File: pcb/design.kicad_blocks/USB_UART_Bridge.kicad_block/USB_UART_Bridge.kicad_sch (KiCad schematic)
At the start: 17 parts, among them J1 614105150721, U2 MCP2221A-I/ST, U3 AP2112K-3.3

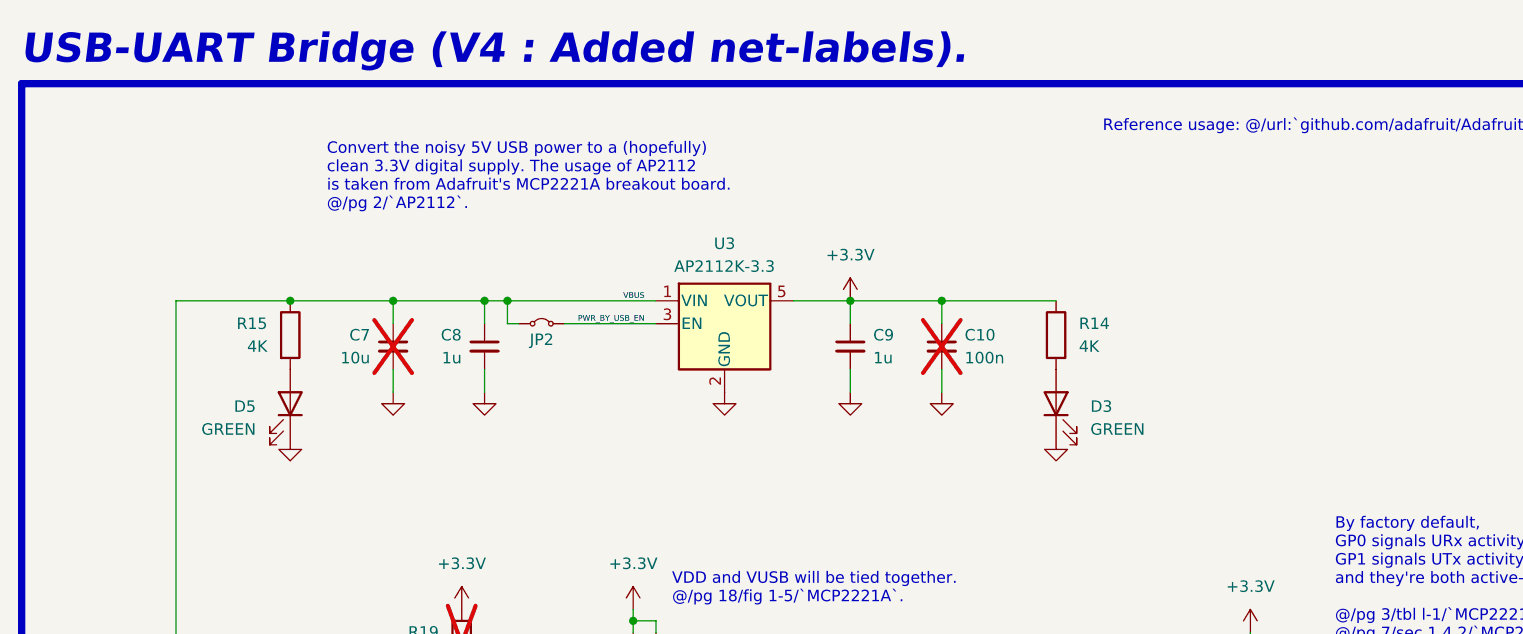
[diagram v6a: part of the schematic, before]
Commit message: Placed down most of the components.
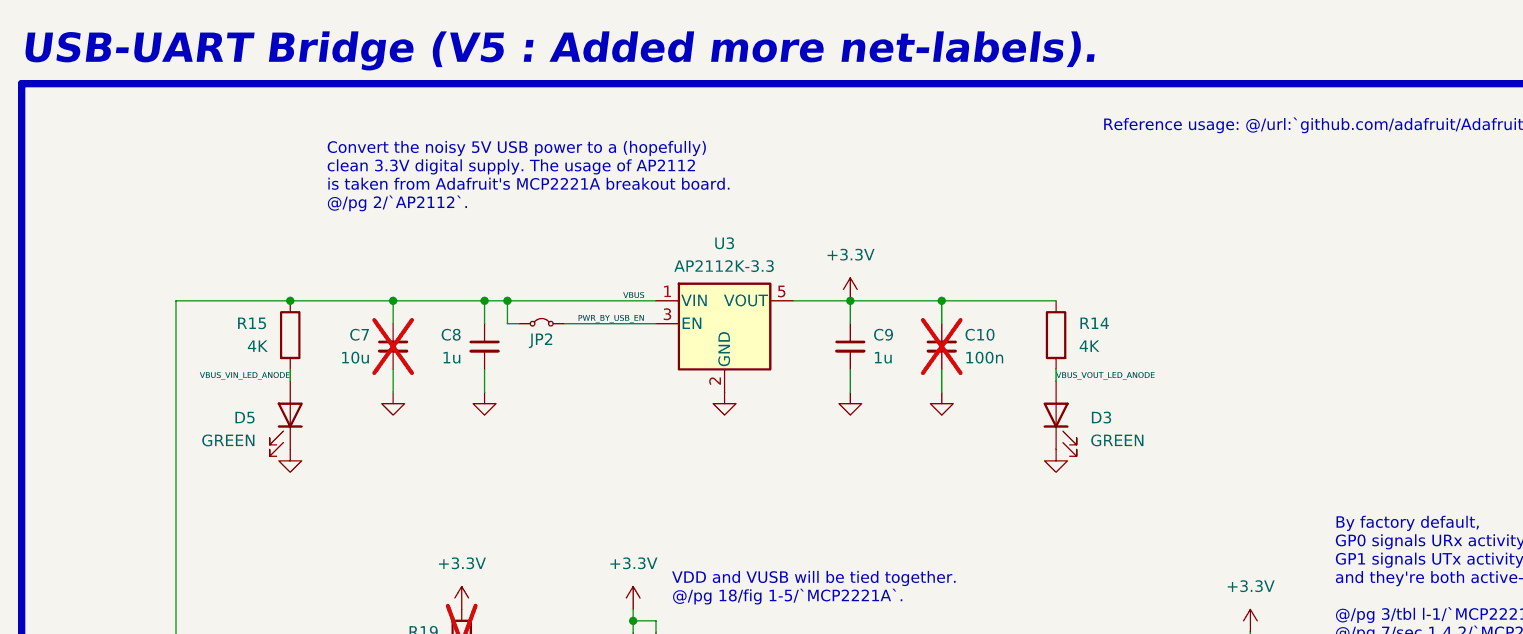
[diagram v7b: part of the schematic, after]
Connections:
- net VBUS_VIN_LED_ANODE: now reaches D5.2 (A), R15.2
- net VBUS_VOUT_LED_ANODE: now reaches D3.2 (A), R14.2
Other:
- note added: "USB-UART Bridge (V5 : Added more net-labels)."
- note removed: "USB-UART Bridge (V4 : Added net-labels)."
- moved on the sheet: D3, D5
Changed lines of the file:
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@@
 		)
 	)
-	(text "USB-UART Bridge (V4 : Added net-labels)."
+	(text "USB-UART Bridge (V5 : Added more net-labels)."
 		(exclude_from_sim no)
 		(at 340.868 43.942 0)
@@
 	(wire
 		(pts
+			(xy 455.93 78.74) (xy 455.93 77.47)
+		)
+		(stroke
+			(width 0)
+			(type default)
+		)
+	)
+	(wire
+		(pts
 			(xy 426.72 69.85) (xy 433.07 69.85)
 		)
@@
 		(pts
 			(xy 347.98 132.08) (xy 350.52 132.08)
+		)
+		(stroke
+			(width 0)
+			(type default)
+		)
+	)
+	(wire
+		(pts
+			(xy 370.84 78.74) (xy 370.84 77.47)
 		)
 		(stroke
@@
 		)
 	)
+	(label "VBUS_VOUT_LED_ANODE"
+		(at 455.93 78.74 0)
+		(effects
+			(font
+				(size 0.635 0.635)
+			)
+			(justify left bottom)
+		)
+	)
 	(label "USB_D-"
 		(at 397.51 124.46 180)
@@
 	(label "VBUS"
 		(at 410.21 69.85 180)
+		(effects
+			(font
+				(size 0.635 0.635)
+			)
+			(justify right bottom)
+		)
+	)
+	(label "VBUS_VIN_LED_ANODE"
+		(at 370.84 78.74 180)
 		(effects
 			(font
@@
 	(symbol
 		(lib_id "Device:LED")
-		(at 370.84 81.28 270)
+		(at 370.84 82.55 270)
 		(mirror x)
 		(unit 1)
@@
 		(dnp no)
 		(property "Reference" "D5"
-			(at 367.03 81.5974 90)
+			(at 367.03 82.8674 90)
 			(effects
 				(font
@@
 		)
 		(property "Value" "GREEN"
-			(at 367.03 84.1374 90)
+			(at 367.03 85.4074 90)
 			(effects
 				(font
@@
 		)
 		(property "Footprint" "LED_SMD:LED_1206_3216Metric_Pad1.42x1.75mm_HandSolder"
-			(at 370.84 81.28 0)
+			(at 370.84 82.55 0)
 			(effects
 				(font
@@
 		)
 		(property "Datasheet" "~"
-			(at 370.84 81.28 0)
+			(at 370.84 82.55 0)
 			(effects
 				(font
@@
 		)
 		(property "Description" "Light emitting diode"
-			(at 370.84 81.28 0)
+			(at 370.84 82.55 0)
 			(effects
 				(font
@@
 		)
 		(property "Sim.Pins" "1=K 2=A"
-			(at 370.84 81.28 0)
+			(at 370.84 82.55 0)
 			(effects
 				(font
@@
 	(symbol
 		(lib_id "power:GND")
-		(at 370.84 85.09 0)
+		(at 370.84 86.36 0)
 		(unit 1)
 		(exclude_from_sim no)
@@
 		(fields_autoplaced yes)
 		(property "Reference" "#PWR040"
+			(at 370.84 92.71 0)
+			(effects
+				(font
+					(size 1.27 1.27)
+				)
+				(hide yes)
+			)
+		)
+		(property "Value" "GND"
 			(at 370.84 91.44 0)
 			(effects
@@
 			)
 		)
-		(property "Value" "GND"
-			(at 370.84 90.17 0)
-			(effects
-				(font
-					(size 1.27 1.27)
-				)
-				(hide yes)
-			)
-		)
 		(property "Footprint" ""
-			(at 370.84 85.09 0)
+			(at 370.84 86.36 0)
 			(effects
 				(font
@@
 		)
 		(property "Datasheet" ""
-			(at 370.84 85.09 0)
+			(at 370.84 86.36 0)
 			(effects
 				(font
@@
 		)
 		(property "Description" "Power symbol creates a global label with name \"GND\" , ground"
-			(at 370.84 85.09 0)
+			(at 370.84 86.36 0)
 			(effects
 				(font
@@
 	(symbol
 		(lib_id "Device:LED")
-		(at 455.93 81.28 90)
+		(at 455.93 82.55 90)
 		(unit 1)
 		(exclude_from_sim no)
@@
 		(dnp no)
 		(property "Reference" "D3"
-			(at 459.74 81.5974 90)
+			(at 459.74 82.8674 90)
 			(effects
 				(font
@@
 		)
 		(property "Value" "GREEN"
-			(at 459.74 84.1374 90)
+			(at 459.74 85.4074 90)
 			(effects
 				(font
@@
 		)
 		(property "Footprint" "LED_SMD:LED_1206_3216Metric_Pad1.42x1.75mm_HandSolder"
-			(at 455.93 81.28 0)
+			(at 455.93 82.55 0)
 			(effects
 				(font
@@
 		)
 		(property "Datasheet" "~"
-			(at 455.93 81.28 0)
+			(at 455.93 82.55 0)
 			(effects
 				(font
@@
 		)
 		(property "Description" "Light emitting diode"
-			(at 455.93 81.28 0)
+			(at 455.93 82.55 0)
 			(effects
 				(font
@@
 		)
 		(property "Sim.Pins" "1=K 2=A"
-			(at 455.93 81.28 0)
+			(at 455.93 82.55 0)
 			(effects
 				(font
@@
 	(symbol
 		(lib_id "power:GND")
-		(at 455.93 85.09 0)
+		(at 455.93 86.36 0)
 		(mirror y)
 		(unit 1)
@@
 		(fields_autoplaced yes)
 		(property "Reference" "#PWR041"
+			(at 455.93 92.71 0)
+			(effects
+				(font
+					(size 1.27 1.27)
+				)
+				(hide yes)
+			)
+		)
+		(property "Value" "GND"
 			(at 455.93 91.44 0)
 			(effects
@@
 			)
 		)
-		(property "Value" "GND"
-			(at 455.93 90.17 0)
-			(effects
-				(font
-					(size 1.27 1.27)
-				)
-				(hide yes)
-			)
-		)
 		(property "Footprint" ""
-			(at 455.93 85.09 0)
+			(at 455.93 86.36 0)
 			(effects
 				(font
@@
 		)
 		(property "Datasheet" ""
-			(at 455.93 85.09 0)
+			(at 455.93 86.36 0)
 			(effects
 				(font
@@
 		)
 		(property "Description" "Power symbol creates a global label with name \"GND\" , ground"
-			(at 455.93 85.09 0)
-			(effects
-				(font
+			(at 455.93 86.36 0)
+			(effects
+				(font

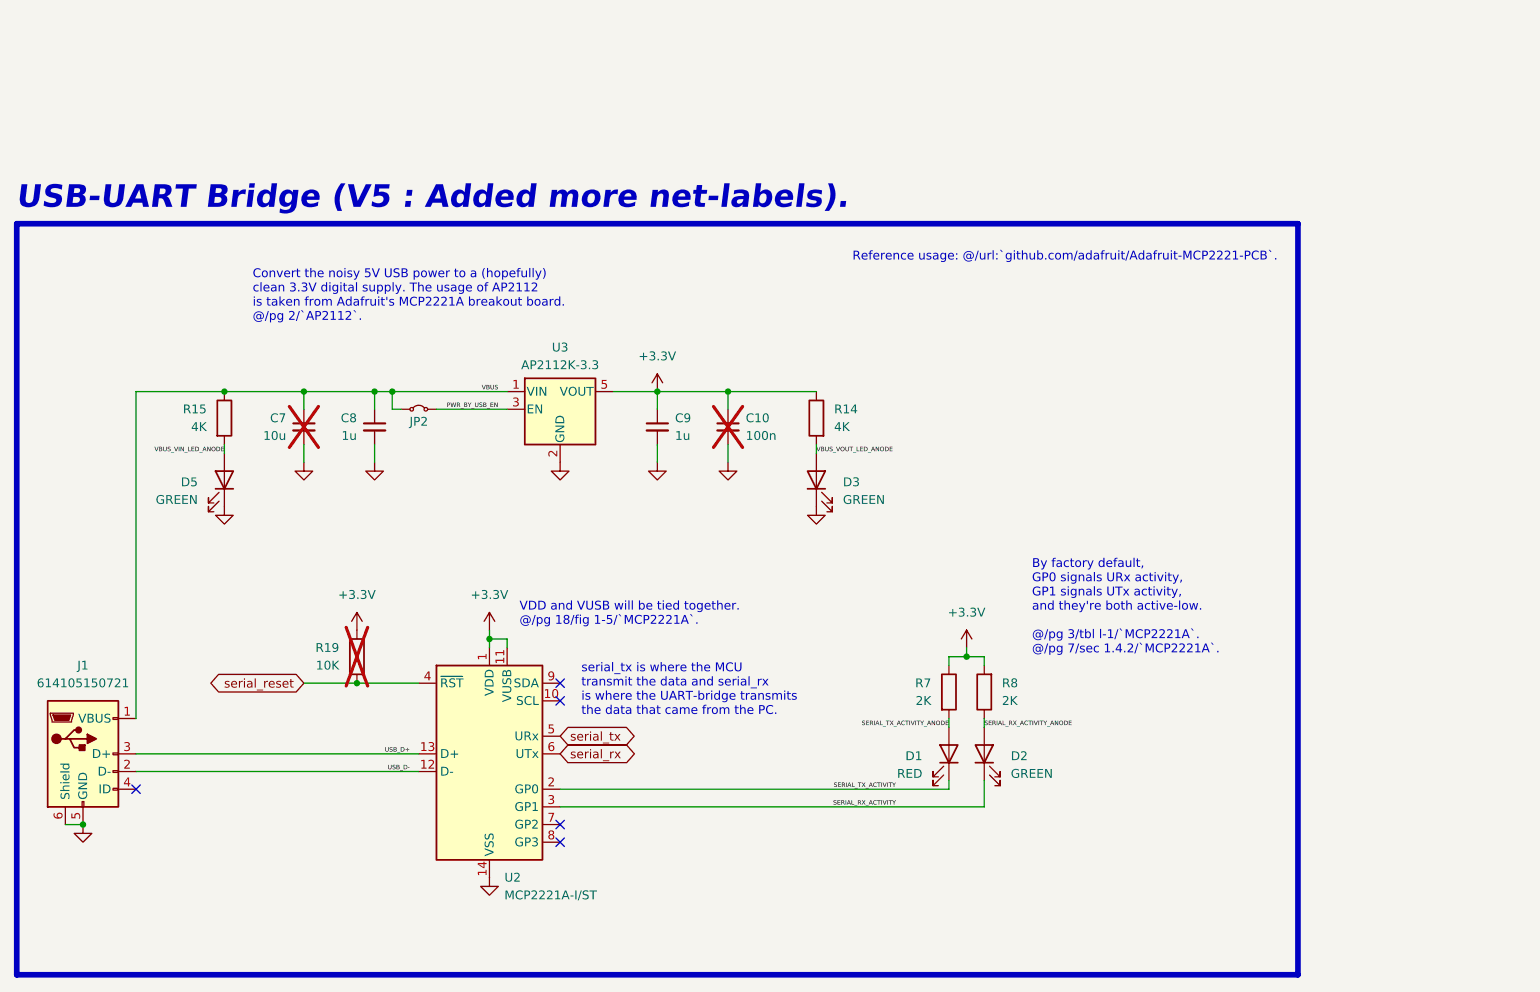
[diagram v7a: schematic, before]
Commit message: `USB-UART Bridge (V6 : USB-C).` : Using USB-C receptacle.
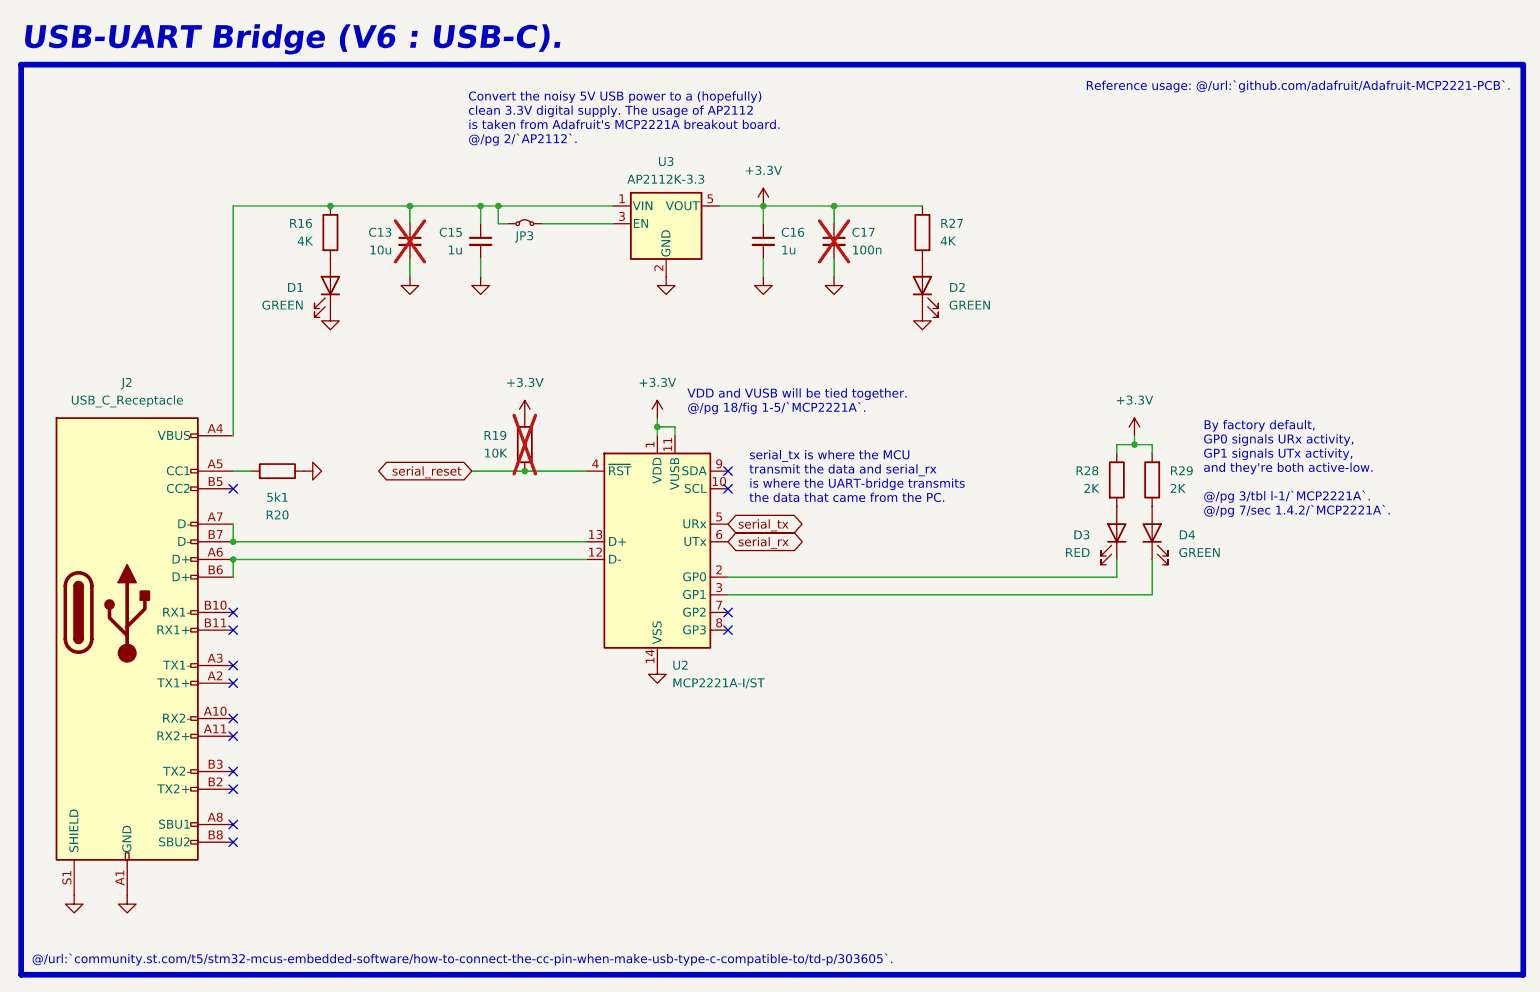
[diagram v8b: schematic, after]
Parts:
- removed J1: 614105150721, pcb:USB_Micro-B_Wuerth_614105150721_Vertical, symbol Connector:USB_B_Micro
- added J2: USB_C_Receptacle, Connector_USB:USB_C_Receptacle_Amphenol_12401548E4-2A, symbol Connector:USB_C_Receptacle
- added R20: 5k1, Resistor_SMD:R_1206_3216Metric_Pad1.30x1.75mm_HandSolder, symbol Device:R
- C13: renamed from C7; now in the parts list
- C17: renamed from C10; now in the parts list
- renumbered C8 to C15, C9 to C16, D5 to D1, D3 to D2, D1 to D3, D2 to D4, JP2 to JP3, R15 to R16, R14 to R27, R7 to R28, R8 to R29
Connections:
- net GND: now also J2.A1 (GND), J2.A12 (GND), J2.B1 (GND), J2.B12 (GND), J2.S1 (SHIELD), R20.1
- net PWR_BY_USB_EN: no longer names the net of JP3.2 (B), U3.3 (EN)
- net SERIAL_RX_ACTIVITY: no longer names the net of D4.1 (K), U2.3 (GP1)
- net SERIAL_RX_ACTIVITY_ANODE: no longer names the net of D4.2 (A), R29.1
- net SERIAL_TX_ACTIVITY: no longer names the net of D3.1 (K), U2.2 (GP0)
- net SERIAL_TX_ACTIVITY_ANODE: no longer names the net of D3.2 (A), R28.2
- net USB_D+: no longer names the net of U2.13 (D+)
- net USB_D+: now also J2.A7 (D-), J2.B7 (D-)
- net USB_D-: no longer names the net of U2.12 (D-)
- net USB_D-: now also J2.A6 (D+), J2.B6 (D+)
- net VBUS: no longer names the net of C13.1, C15.1, JP3.1 (A), R16.1, U3.1 (VIN)
- net VBUS: now also J2.A4 (VBUS), J2.A9 (VBUS), J2.B4 (VBUS), J2.B9 (VBUS)
- net VBUS_VIN_LED_ANODE: no longer names the net of D1.2 (A), R16.2
- net VBUS_VOUT_LED_ANODE: no longer names the net of D2.2 (A), R27.2
- new net: J2.A5 (CC1), R20.2
- no-connect marks 5 -> 15
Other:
- note added: "@/url:`community.st.com/t5/stm32-mcus-embedded-software/how-to-connect-the-cc-pin-when-make-usb-type-c-compatible-to/td-p/303605`."
- note added: "USB-UART Bridge (V6 : USB-C)."
- note removed: "USB-UART Bridge (V5 : Added more net-labels)."
- moved on the sheet: C13, C15, C16, C17, D1, D2, D3, D4, JP3, R16, R19, R27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
